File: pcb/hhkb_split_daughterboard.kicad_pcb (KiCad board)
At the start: 2 copper layers, 21 x 32 mm, 11 parts

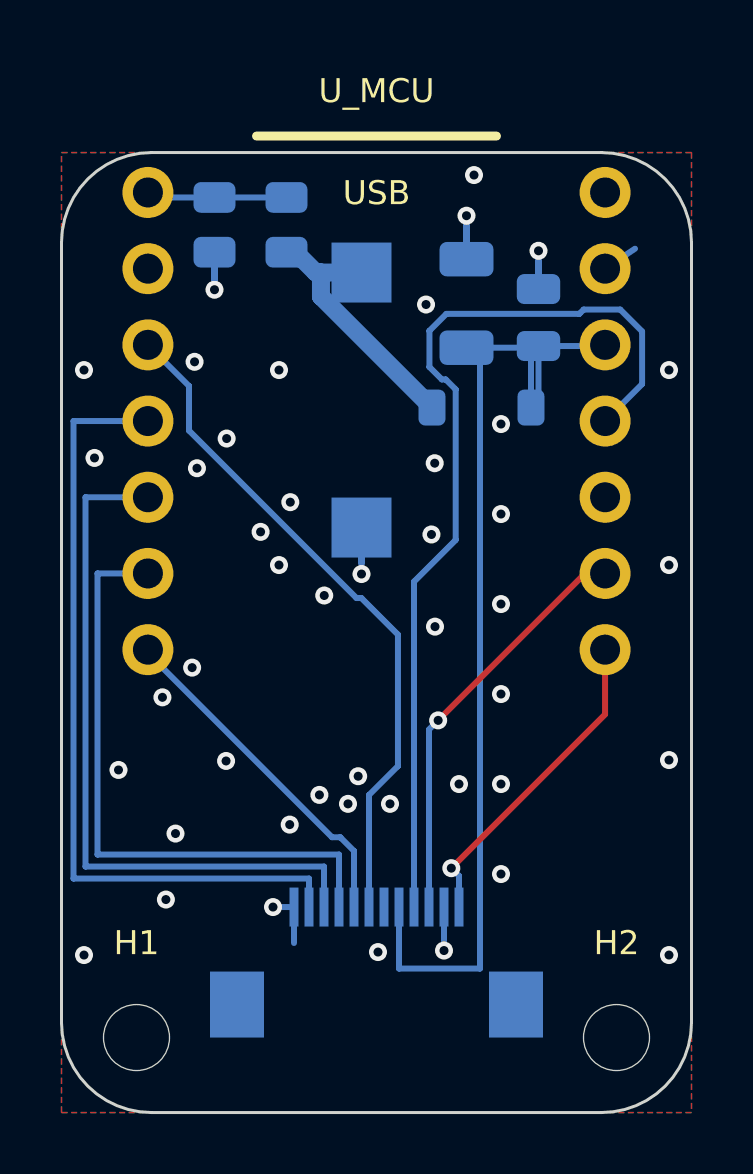
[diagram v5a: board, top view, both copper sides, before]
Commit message: 外周レーンを板端とパッドのまん中に置いた
**配線が板の端ギリギリだった**（利用者の指摘）。ROW2 の銅から板端まで
**0.30mm ＝ 設計規則ちょうど**で、丸め 1 つで割れる余裕しかなかった。
レーンを `outer_limit`（板端 + 端クリアランス）から配っていたため。

⚠️ **パッド側へ寄せるのでは直らない。**そうすると今度は ROW4 が D6 の
パッドまで 0.20mm（これも規則ちょうど）になる（利用者「右に寄りすぎ。
D5 のラインが D6 の絶縁に被ってます」）。

⚠️ **クリアランスを足した内側で中央を取っても、まん中にならない。**
板端側は端クリアランス 0.30、パッド側は銅間クリアランス 0.20 と
**足す量が違う**ので、その差 0.10mm がそのまま偏りになる
（実測: 板端 0.56mm に対しパッド側 0.46mm）。

**障害物の縁そのもの**（板端 -10.50 と パッドの左端 -8.47）でまん中を
取り、そこへ束の中心を置く（利用者「絶縁部も含めて中央揃えが正しい
のでは」）。

    板端まで **0.515mm** / パッド縁まで **0.515mm**（差 0.000）

規則（板端 0.30・銅間 0.20）に対して両側とも 1.7〜2.6 倍。

順序と形は変えていない: ROW2 が最も外周（-9.88 / -9.49 / -9.09）、
交差 0・斜め 0・折れ 3 回。違反 0 / 未配線 0 / 警告 16。

Co-Authored-By: Claude Opus 5 (1M context) <noreply@anthropic.com>
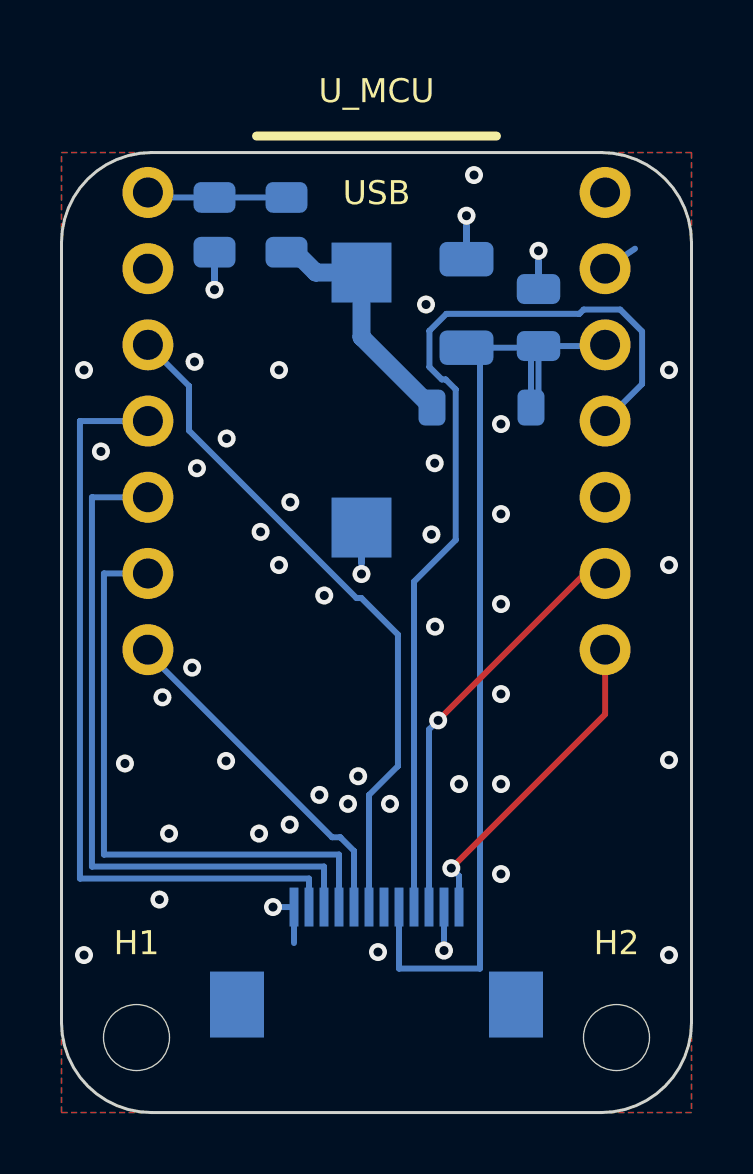
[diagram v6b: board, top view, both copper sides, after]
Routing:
- net VBATT_SW: track 8.81 -> 8.25 mm
- net GND: vias 45 -> 46

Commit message: D2 と D6 も列の内側を L 字で FFC へ引いた
ROW0/ROW1 は Freerouting 任せで盤面を斜めに横断していた（ROW0 は
直線 22.4mm に対し 39.1mm）。ROW2/3/4 と同じ理屈で自分で引く。

  D6（ROW1）… 垂直に下ろす → 直角に曲げて FFC へ
  D2（ROW0）… D5 と同じ 1.465mm だけ逆向き（右）へ水平に伸ばす
              → 垂直に下ろす → 直角に曲げて FFC へ

途中で 2 つ間違えたので、両方コメントに残した:

1. 横枝の帯を ROW2/3/4 と同じ lo..hi に取り、外周組の帯と FFC の
   パッドの両方より下へ降りた。縦の 2 本が横の 3 本を突き抜けて
   不要な交差が 7 件。帯は外周組より上に取る。

2.「D5 と同じ長さ」を ROW4 の水平区間の max で拾い、パッドから出る
   枝（1.465mm）ではなく FFC 近くの帯（7.835mm）を掴んだ。その先が
   BT1_- のパッドの真上で短絡。MCU のパッドに接する方だけを見る。

autoroute.PREWIRED_DB に ROW[01] を追加（protect にしないと
Freerouting が二重に引いて自己交差する）。

daughterboard: DRC 違反 0 / 未配線 0 / B.Cu 全ネットの交差 0。
左右の基板は触っていない。

Co-Authored-By: Claude Opus 5 (1M context) <noreply@anthropic.com>
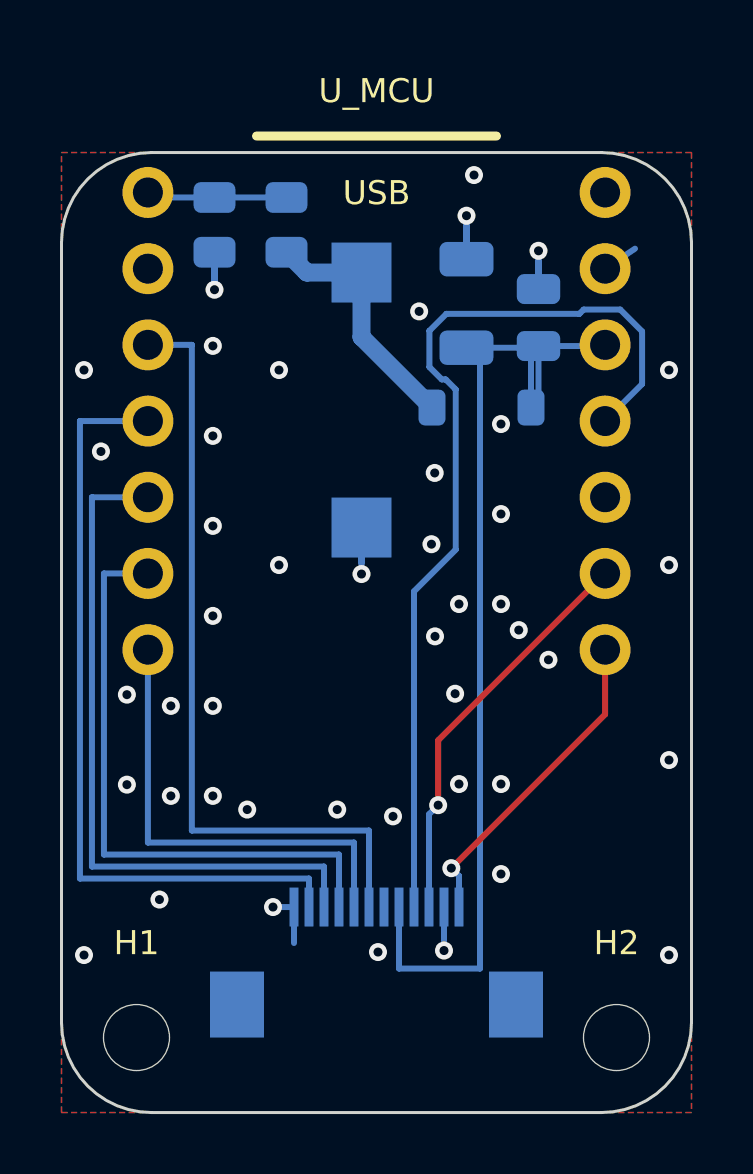
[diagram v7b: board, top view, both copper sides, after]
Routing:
- net ROW1: track 11.6 -> 15.5 mm
- net ROW0: track 22.7 -> 26.1 mm
- net GND: vias 46 -> 45

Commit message: 子基板の FFC 7〜12 を組み替え、レーンを XIAO のパッドで持つようにした
利用者の指定で、XIAO のパッド列の内側と外側を入れ替えた。列の外は
D1（最も板端）→ D2 → D3、内側は D6（垂直）→ D5 → D4。そのうえで
FFC の 7〜12 を 1 つずらし、載る信号を XIAO 側で吸収した。

    7 SPARE(D4) / 8 ROW3(D5) / 9 ROW4(D6)
    10 ROW1(D3) / 11 ROW2(D2) / 12 ROW0(D1)

D1 は用途未定のまま FFC 12 番まで配線だけ通す（後から線は足せない）。
GND の 2 本目は 12 番から 6 番へ移した。

レーンの表を ROW 名で持っていたのをやめ、**XIAO のパッド番号**で持つ
ようにした（OUTER_LANE_PADS / INNER_LANE_PADS / VERTICAL_PAD）。
どのレーンを通るかはパッドの話で、そこに載る信号とは無関係。ROW 名で
書いていたために、内外を入れ替えた時点で表と実物がずれ、D4 と D5 が
同じ x に降りて交差を 2 件出した。ネット名はパッドから引く。

内側が 2 本以上になったので、降りる x も帯と同じピッチでずらす。
ファームの row-gpios と決定記録の表も追随させた。

子基板 DRC: 未配線 0 / 違反 1（V3V3 と GND ビアが 0.100mm。利用者の
指示で保留）。主基板の SPARE が片側 1 ピンなので test_circuit が 2 件
赤。左右の基板は FFC が固まってから直す。

Co-Authored-By: Claude Opus 5 (1M context) <noreply@anthropic.com>
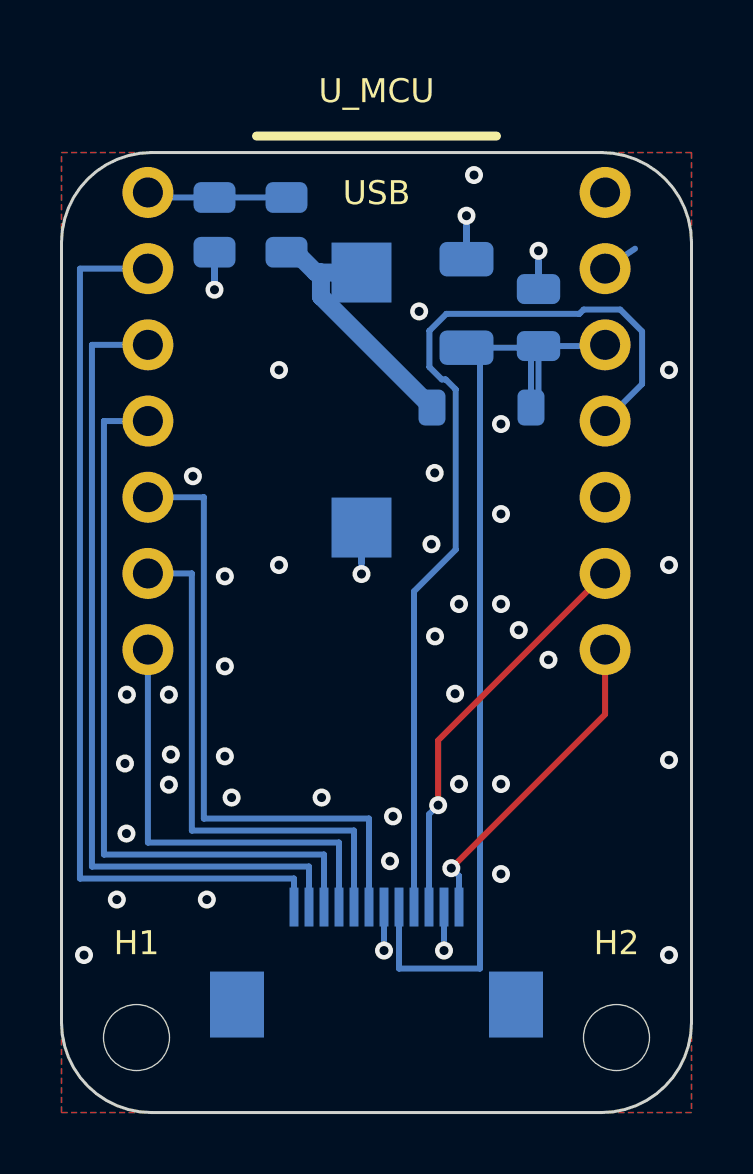
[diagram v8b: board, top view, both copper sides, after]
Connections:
- J_MAIN pad 10: ROW3 -> ROW1
- J_MAIN pad 12: GND -> ROW0
- J_MAIN pad 6: (no net) -> GND
- J_MAIN pad 7: ROW0 -> SPARE
- J_MAIN pad 8: ROW1 -> ROW3
- U_MCU pad D1: (no net) -> ROW0
- U_MCU pad D2: ROW0 -> ROW2
- U_MCU pad D3: ROW2 -> ROW1
- U_MCU pad D4: ROW3 -> SPARE
- U_MCU pad D5: ROW4 -> ROW3
- U_MCU pad D6: ROW1 -> ROW4
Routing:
- net SPARE: track 0.00 -> 21.0 mm
- net ROW1: track 15.5 -> 25.0 mm
- net ROW4: track 20.4 -> 15.0 mm
- net ROW3: track 23.3 -> 18.0 mm
- net ROW0: track 26.1 -> 30.7 mm
- net ROW2: track 26.1 -> 27.8 mm
- net GND: track 16.1 -> 16.8 mm, vias 45 -> 44
- net VBATT_SW: track 8.25 -> 8.81 mm
